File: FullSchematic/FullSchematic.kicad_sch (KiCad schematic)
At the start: 1 part, among them Q1 PMOS

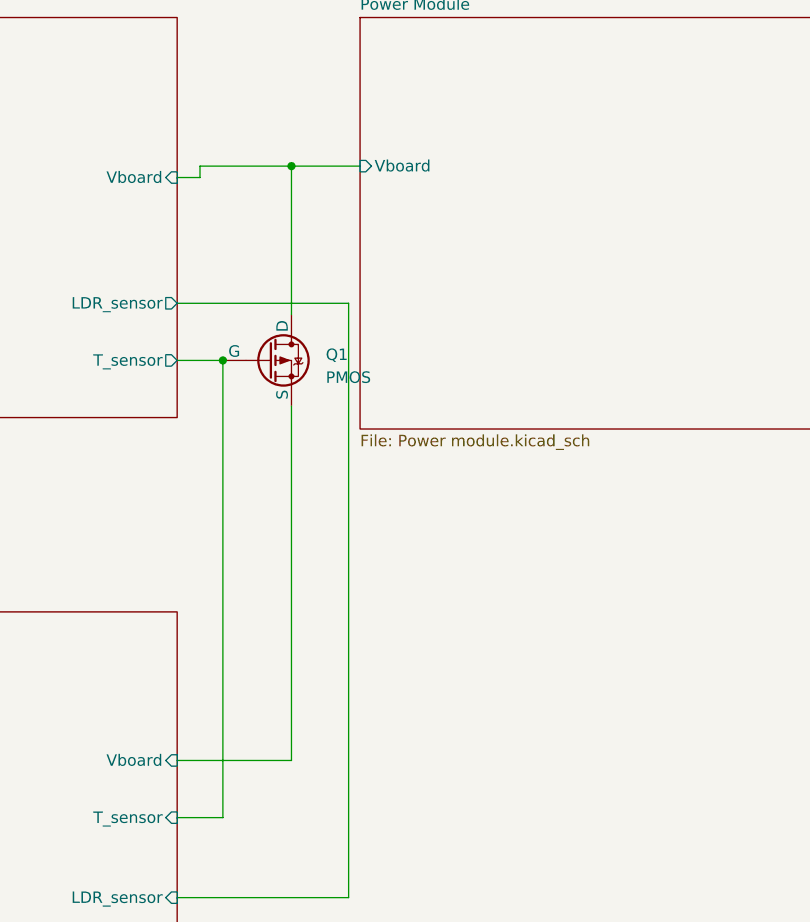
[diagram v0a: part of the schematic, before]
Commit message: Added uvlo circuit
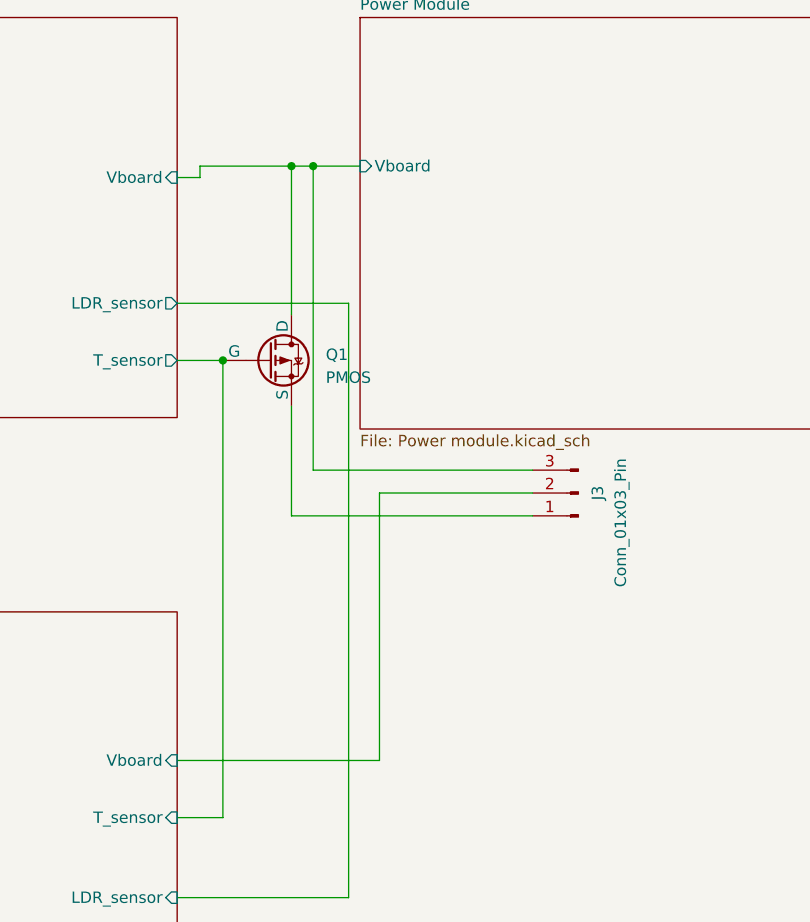
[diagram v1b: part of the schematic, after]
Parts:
- added J3: Conn_01x03_Pin, Connector_PinHeader_1.00mm:PinHeader_1x03_P1.00mm_Vertical, symbol Connector:Conn_01x03_Pin
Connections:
- net Microcontroller/Vboard: now also J3.2 (Pin_2); no longer Q1.3 (S)
- net Power Module/Vboard: now also J3.3 (Pin_3)
- new net: J3.1 (Pin_1), Q1.3 (S)
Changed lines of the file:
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@@
   (junction (at 167.64 49.53) (diameter 0) (color 0 0 0 0)
   )
+  (junction (at 170.053 49.53) (diameter 0) (color 0 0 0 0)
+  )
   (junction (at 160.02 71.12) (diameter 0) (color 0 0 0 0)
+  )
+  (wire (pts (xy 177.419 85.852) (xy 194.437 85.852))
+    (stroke (width 0) (type default))
   )
   (wire (pts (xy 233.68 138.43) (xy 233.68 78.74))
     (stroke (width 0) (type default))
   )
+  (wire (pts (xy 170.053 83.312) (xy 194.437 83.312))
+    (stroke (width 0) (type default))
+  )
+  (wire (pts (xy 167.64 49.53) (xy 167.64 66.04))
+    (stroke (width 0) (type default))
+  )
   (wire (pts (xy 157.48 49.53) (xy 157.48 50.8))
+    (stroke (width 0) (type default))
+  )
+  (wire (pts (xy 167.64 76.2) (xy 167.64 88.392))
     (stroke (width 0) (type default))
   )
@@
     (stroke (width 0) (type default))
   )
-  (wire (pts (xy 167.64 49.53) (xy 167.64 66.04))
+  (wire (pts (xy 170.053 49.53) (xy 175.26 49.53))
+    (stroke (width 0) (type default))
+  )
+  (wire (pts (xy 167.64 49.53) (xy 170.053 49.53))
     (stroke (width 0) (type default))
   )
@@
     (stroke (width 0) (type default))
   )
-  (wire (pts (xy 157.48 49.53) (xy 167.64 49.53))
-    (stroke (width 0) (type default))
-  )
   (wire (pts (xy 154.94 121.92) (xy 160.02 121.92))
     (stroke (width 0) (type default))
   )
-  (wire (pts (xy 154.94 115.57) (xy 167.64 115.57))
-    (stroke (width 0) (type default))
-  )
-  (wire (pts (xy 167.64 49.53) (xy 175.26 49.53))
+  (wire (pts (xy 157.48 49.53) (xy 167.64 49.53))
     (stroke (width 0) (type default))
   )
@@
     (stroke (width 0) (type default))
   )
+  (wire (pts (xy 154.94 115.57) (xy 177.419 115.57))
+    (stroke (width 0) (type default))
+  )
+  (wire (pts (xy 167.64 88.392) (xy 194.437 88.392))
+    (stroke (width 0) (type default))
+  )
   (wire (pts (xy 173.99 130.81) (xy 154.94 130.81))
     (stroke (width 0) (type default))
   )
-  (wire (pts (xy 167.64 76.2) (xy 167.64 115.57))
+  (wire (pts (xy 170.053 49.53) (xy 170.053 83.312))
+    (stroke (width 0) (type default))
+  )
+  (wire (pts (xy 177.419 85.852) (xy 177.419 115.57))
     (stroke (width 0) (type default))
   )
@@
         )
       )
+    )
+  )
+  (symbol (lib_id "Connector:Conn_01x03_Pin") (at 199.517 85.852 180) (unit 1)
+    (in_bom yes) (on_board yes) (dnp no)
+    (property "Reference" "J3" (at 201.676 85.852 90)
+      (effects (font (size 1.27 1.27)))
+    )
+    (property "Value" "Conn_01x03_Pin" (at 204.216 89.154 90)
+      (effects (font (size 1.27 1.27)))
+    )
+    (property "Footprint" "Connector_PinHeader_1.00mm:PinHeader_1x03_P1.00mm_Vertical" (at 199.517 85.852 0)
+      (effects (font (size 1.27 1.27)) hide)
+    )
+    (property "Datasheet" "~" (at 199.517 85.852 0)
+      (effects (font (size 1.27 1.27)) hide)
+    )
+    (pin "1")
+    (pin "2")
+    (pin "3")
+    (instances
+      (project "FullSchematic"
+        (path "/5dd86611-a33d-45ee-946c-01c599f30b12"
+          (reference "J3") (unit 1)
+        )
+      )

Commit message: Confirmed part numbers and prices
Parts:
- added Q3: IRLML6402, Package_TO_SOT_SMD:SOT-23, symbol Simulation_SPICE:PMOS
- added Q4: 2N7002, Package_TO_SOT_SMD:SOT-23, symbol Transistor_FET:2N7002
- J3: footprint Connector_PinHeader_1.00mm:PinHeader_1x03_P1.00mm_Vertical -> Connector_PinHeader_2.54mm:PinHeader_1x03_P2.54mm_Vertical; JLCPCB Part # (none) -> N/A; Populate (none) -> No; Price (none) -> N/A; Price ( 1 board) (none) -> N/A; Price (5 boards) (none) -> N/A
- Q1: value PMOS -> IRLML6402; footprint Package_TO_SOT_THT:TO-3P-3_Vertical -> Package_TO_SOT_SMD:SOT-23; JLCPCB Part # C115991 -> C518785; Populate (none) -> Yes; Price 0.52 -> 0.5; Price ( 1 board) 0.52 -> 0.5; Price (5 boards) 2.6 -> 0.25
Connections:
- net Pin 1: now reaches J3.1 (Pin_1), Q1.3 (S)
- net Microcontroller/T_sensor: no longer names the net of Q1.2 (G)
- net Microcontroller/T_sensor: now also Q3.3 (S), Q4.3 (D)
- net Power Module/Vboard renamed Vboard
- net Vboard: now also Q3.1 (D)
- new net GND: Q4.2 (S)
- new net Output of Touch Sensor: Q3.2 (G), Q4.1 (G)

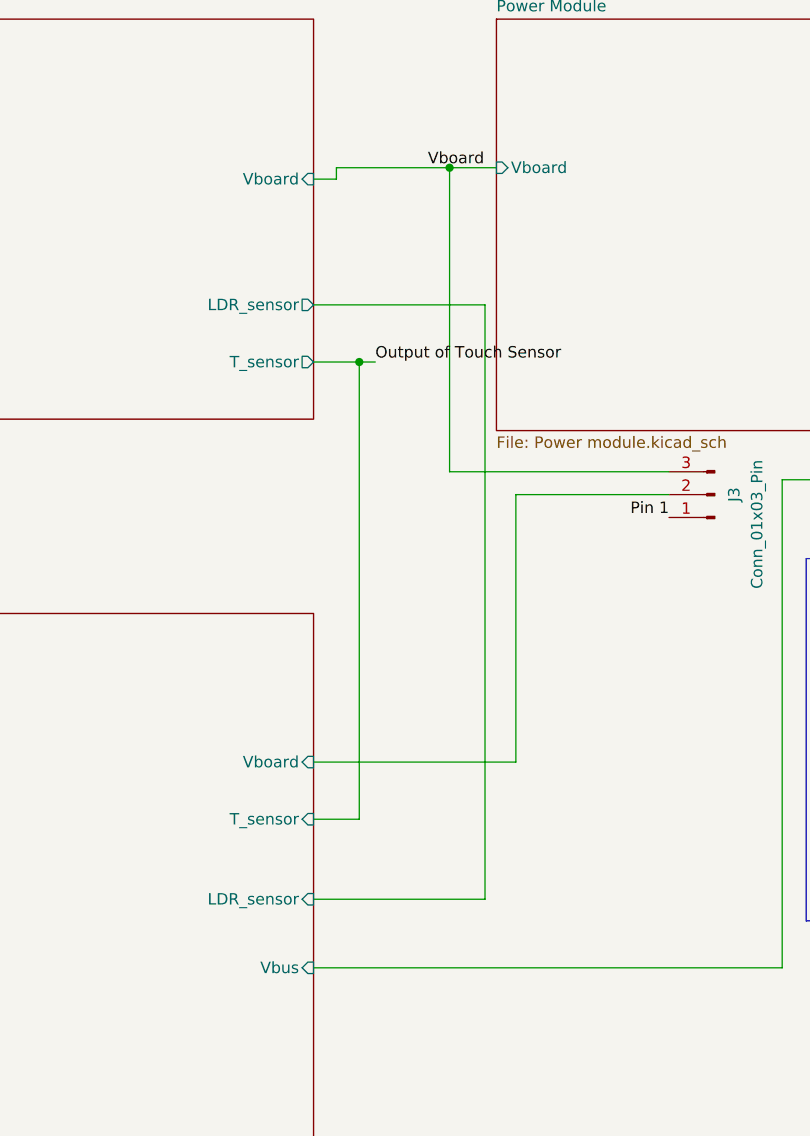
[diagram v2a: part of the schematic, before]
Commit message: Checked part #s, prices, footprints
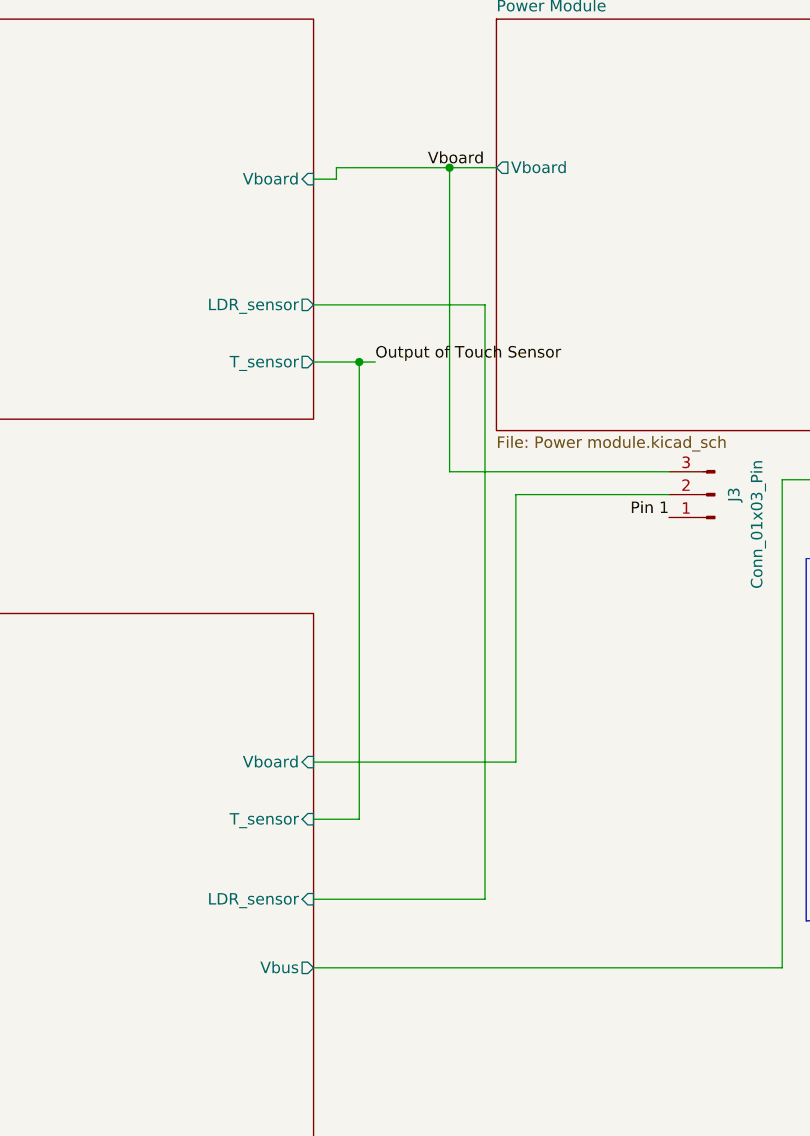
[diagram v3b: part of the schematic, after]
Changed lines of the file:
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@@
       (effects (font (size 1.27 1.27)) hide)
     )
-    (pin "Vboard" input (at 175.26 49.53 180)
+    (pin "Vboard" output (at 175.26 49.53 180)
       (effects (font (size 1.27 1.27)) (justify left))
     )
@@
       (effects (font (size 1.27 1.27)) (justify right))
     )
-    (pin "Vbus" input (at 154.94 138.43 0)
+    (pin "Vbus" output (at 154.94 138.43 0)
       (effects (font (size 1.27 1.27)) (justify right))
     )

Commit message: generated files
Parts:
- J3: JLCPCB Part # N/A -> (none)
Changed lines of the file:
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@@
       (effects (font (size 1.27 1.27)) hide)
     )
-    (property "JLCPCB Part #" "N/A" (at 199.517 85.852 0)
+    (property "JLCPCB Part #" "" (at 199.517 85.852 0)
       (effects (font (size 1.27 1.27)) hide)
     )

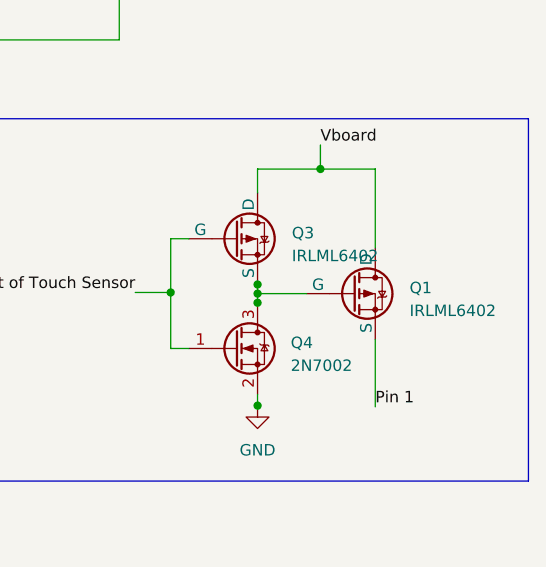
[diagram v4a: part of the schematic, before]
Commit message: Decreased Price
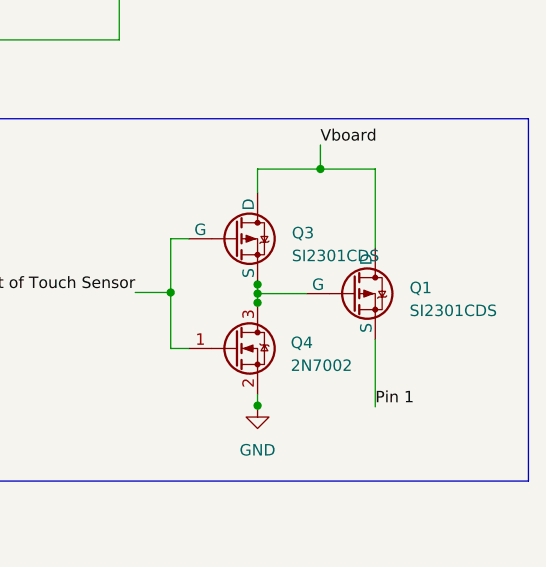
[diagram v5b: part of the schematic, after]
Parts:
- Q1, Q3: value IRLML6402 -> SI2301CDS; JLCPCB Part # C518785 -> C10487
- Q4: JLCPCB Part # C111971 -> C8545
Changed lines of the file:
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@@
       (effects (font (size 1.27 1.27)) (justify left) hide)
     )
-    (property "JLCPCB Part #" "C111971" (at 246.507 118.491 0)
+    (property "JLCPCB Part #" "C8545" (at 246.507 118.491 0)
       (effects (font (size 1.27 1.27)) hide)
     )
@@
       (effects (font (size 1.27 1.27)) (justify left))
     )
-    (property "Value" "IRLML6402" (at 265.938 114.3 0)
+    (property "Value" "SI2301CDS" (at 265.938 114.3 0)
       (effects (font (size 1.27 1.27)) (justify left))
     )
@@
       (effects (font (size 1.27 1.27)) hide)
     )
-    (property "JLCPCB Part #" "C518785" (at 259.588 112.395 0)
+    (property "JLCPCB Part #" "C10487" (at 259.588 112.395 0)
       (effects (font (size 1.27 1.27)) hide)
     )
@@
       (effects (font (size 1.27 1.27)) (justify left))
     )
-    (property "Value" "IRLML6402" (at 252.857 108.204 0)
+    (property "Value" "SI2301CDS" (at 252.857 108.204 0)
       (effects (font (size 1.27 1.27)) (justify left))
     )
@@
       (effects (font (size 1.27 1.27)) hide)
     )
-    (property "JLCPCB Part #" "C518785" (at 246.507 106.299 0)
+    (property "JLCPCB Part #" "C10487" (at 246.507 106.299 0)
       (effects (font (size 1.27 1.27)) hide)
     )

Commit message: Uploaded final board design
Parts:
- removed J3: Conn_01x03_Pin, Connector_PinHeader_2.54mm:PinHeader_1x03_P2.54mm_Vertical, symbol Connector:Conn_01x03_Pin
- added J3: Conn_01x04_Pin, Connector_PinHeader_2.54mm:PinHeader_1x04_P2.54mm_Vertical, symbol Connector:Conn_01x04_Pin
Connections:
- net Microcontroller/Vboard: now also J3.3 (Pin_3)
- net Vboard: now also J3.4 (Pin_4)
- net Pin 1 renamed Pin 2
- net Pin 2: now also J3.2 (Pin_2)
- new net Microcontroller/T_sensor: J3.1 (Pin_1)
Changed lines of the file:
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@@
     (comment 3 "Kudzi Kadzimu (KDZKUD001)")
   )
-  (junction (at 249.047 111.379) (diameter 0) (color 0 0 0 0)
-  )
-  (junction (at 249.047 113.411) (diameter 0) (color 0 0 0 0)
+  (junction (at 249.047 112.395) (diameter 0) (color 0 0 0 0)
   )
   (junction (at 170.053 49.53) (diameter 0) (color 0 0 0 0)
@@
   (junction (at 239.395 112.268) (diameter 0) (color 0 0 0 0)
   )
-  (junction (at 249.047 112.395) (diameter 0) (color 0 0 0 0)
-  )
   (junction (at 256.032 98.552) (diameter 0) (color 0 0 0 0)
-  )
-  (junction (at 249.047 124.841) (diameter 0) (color 0 0 0 0)
-  )
-  (junction (at 160.02 71.12) (diameter 0) (color 0 0 0 0)
-  )
-  (wire (pts (xy 249.047 123.571) (xy 249.047 124.841))
-    (stroke (width 0) (type default))
   )
   (wire (pts (xy 207.01 138.43) (xy 154.94 138.43))
@@
     (stroke (width 0) (type default))
   )
-  (wire (pts (xy 249.047 112.395) (xy 249.047 113.411))
-    (stroke (width 0) (type default))
-  )
   (wire (pts (xy 239.395 118.491) (xy 241.427 118.491))
     (stroke (width 0) (type default))
@@
     (stroke (width 0) (type default))
   )
+  (wire (pts (xy 249.047 123.571) (xy 249.047 124.841))
+    (stroke (width 0) (type default))
+  )
   (wire (pts (xy 233.68 78.74) (xy 233.68 84.201))
     (stroke (width 0) (type default))
   )
-  (wire (pts (xy 161.798 71.12) (xy 160.02 71.12))
+  (wire (pts (xy 154.94 71.12) (xy 161.798 71.12))
     (stroke (width 0) (type default))
   )
@@
     (stroke (width 0) (type default))
   )
-  (wire (pts (xy 249.047 124.841) (xy 249.047 124.968))
-    (stroke (width 0) (type default))
-  )
   (wire (pts (xy 256.032 95.885) (xy 256.032 98.552))
     (stroke (width 0) (type default))
   )
-  (wire (pts (xy 249.047 111.379) (xy 249.047 112.395))
+  (wire (pts (xy 249.047 112.395) (xy 249.047 113.411))
     (stroke (width 0) (type default))
   )
   (wire (pts (xy 262.128 124.968) (xy 262.128 117.475))
-    (stroke (width 0) (type default))
-  )
-  (wire (pts (xy 249.047 111.252) (xy 249.047 111.379))
     (stroke (width 0) (type default))
   )
@@
     (stroke (width 0) (type default))
   )
-  (wire (pts (xy 249.047 113.538) (xy 249.174 113.538))
-    (stroke (width 0) (type default))
-  )
-  (wire (pts (xy 249.174 113.411) (xy 249.174 113.538))
-    (stroke (width 0) (type default))
-  )
   (wire (pts (xy 173.99 64.77) (xy 173.99 130.81))
-    (stroke (width 0) (type default))
-  )
-  (wire (pts (xy 249.047 113.411) (xy 249.047 113.538))
     (stroke (width 0) (type default))
   )
@@
     (stroke (width 0) (type default))
   )
-  (wire (pts (xy 154.94 121.92) (xy 160.02 121.92))
+  (wire (pts (xy 154.94 121.92) (xy 194.437 121.92))
     (stroke (width 0) (type default))
   )
@@
     (stroke (width 0) (type default))
   )
-  (wire (pts (xy 154.94 71.12) (xy 160.02 71.12))
+  (wire (pts (xy 249.047 112.395) (xy 254.508 112.395))
     (stroke (width 0) (type default))
   )
@@
   )
   (wire (pts (xy 249.047 101.219) (xy 249.047 98.552))
+    (stroke (width 0) (type default))
+  )
+  (wire (pts (xy 194.437 90.932) (xy 194.437 121.92))
     (stroke (width 0) (type default))
   )
@@
     (stroke (width 0) (type default))
   )
-  (wire (pts (xy 249.047 112.395) (xy 254.508 112.395))
-    (stroke (width 0) (type default))
-  )
   (wire (pts (xy 262.128 98.552) (xy 262.128 107.315))
-    (stroke (width 0) (type default))
-  )
-  (wire (pts (xy 160.02 71.12) (xy 160.02 121.92))
     (stroke (width 0) (type default))
   )
@@
   )
   (wire (pts (xy 241.427 106.299) (xy 239.395 106.299))
+    (stroke (width 0) (type default))
+  )
+  (wire (pts (xy 249.047 111.379) (xy 249.047 112.395))
     (stroke (width 0) (type default))
   )
@@
     (effects (font (size 1.27 1.27)) (justify left bottom))
   )
-  (label "Pin 1" (at 194.437 88.392 180) (fields_autoplaced)
-    (effects (font (size 1.27 1.27)) (justify right bottom))
-  )
-  (label "Pin 1" (at 262.128 124.968 0) (fields_autoplaced)
+  (label "Pin 2" (at 262.128 124.968 0) (fields_autoplaced)
     (effects (font (size 1.27 1.27)) (justify left bottom))
   )
@@
   )
   (label "Output of Touch Sensor" (at 235.458 112.268 180) (fields_autoplaced)
+    (effects (font (size 1.27 1.27)) (justify right bottom))
+  )
+  (label "Pin 2" (at 194.437 88.392 180) (fields_autoplaced)
     (effects (font (size 1.27 1.27)) (justify right bottom))
   )
@@
     )
   )
-  (symbol (lib_id "Connector:Conn_01x03_Pin") (at 199.517 85.852 180) (unit 1)
-    (in_bom yes) (on_board yes) (dnp no)
-    (property "Reference" "J3" (at 201.676 85.852 90)
-      (effects (font (size 1.27 1.27)))
+  (symbol (lib_id "Connector:Conn_01x04_Pin") (at 199.517 88.392 180) (unit 1)
+    (in_bom yes) (on_board yes) (dnp no) (fields_autoplaced)
+    (property "Reference" "J3" (at 200.66 86.487 0)
+      (effects (font (size 1.27 1.27)) (justify right))
     )
-    (property "Value" "Conn_01x03_Pin" (at 204.216 89.154 90)
-      (effects (font (size 1.27 1.27)))
+    (property "Value" "Conn_01x04_Pin" (at 200.66 89.027 0)
+      (effects (font (size 1.27 1.27)) (justify right))
     )
-    (property "Footprint" "Connector_PinHeader_2.54mm:PinHeader_1x03_P2.54mm_Vertical" (at 199.517 85.852 0)
+    (property "Footprint" "Connector_PinHeader_2.54mm:PinHeader_1x04_P2.54mm_Vertical" (at 199.517 88.392 0)
       (effects (font (size 1.27 1.27)) hide)
     )
-    (property "Datasheet" "~" (at 199.517 85.852 0)
-      (effects (font (size 1.27 1.27)) hide)
-    )
-    (property "JLCPCB Part #" "" (at 199.517 85.852 0)
-      (effects (font (size 1.27 1.27)) hide)
-    )
-    (property "Populate" "No" (at 199.517 85.852 0)
-      (effects (font (size 1.27 1.27)) hide)
-    )
-    (property "Price" "N/A" (at 199.517 85.852 0)
-      (effects (font (size 1.27 1.27)) hide)
-    )
-    (property "Price ( 1 board)" "N/A" (at 199.517 85.852 0)
-      (effects (font (size 1.27 1.27)) hide)
-    )
-    (property "Price (5 boards)" "N/A" (at 199.517 85.852 0)
+    (property "Datasheet" "~" (at 199.517 88.392 0)
       (effects (font (size 1.27 1.27)) hide)
     )
@@
     (pin "2")
     (pin "3")
+    (pin "4")
     (instances
       (project "FullSchematic"
